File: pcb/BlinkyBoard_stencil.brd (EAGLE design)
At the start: 25.2 x 10 mm, 23 parts, among them Q1 16 MHz

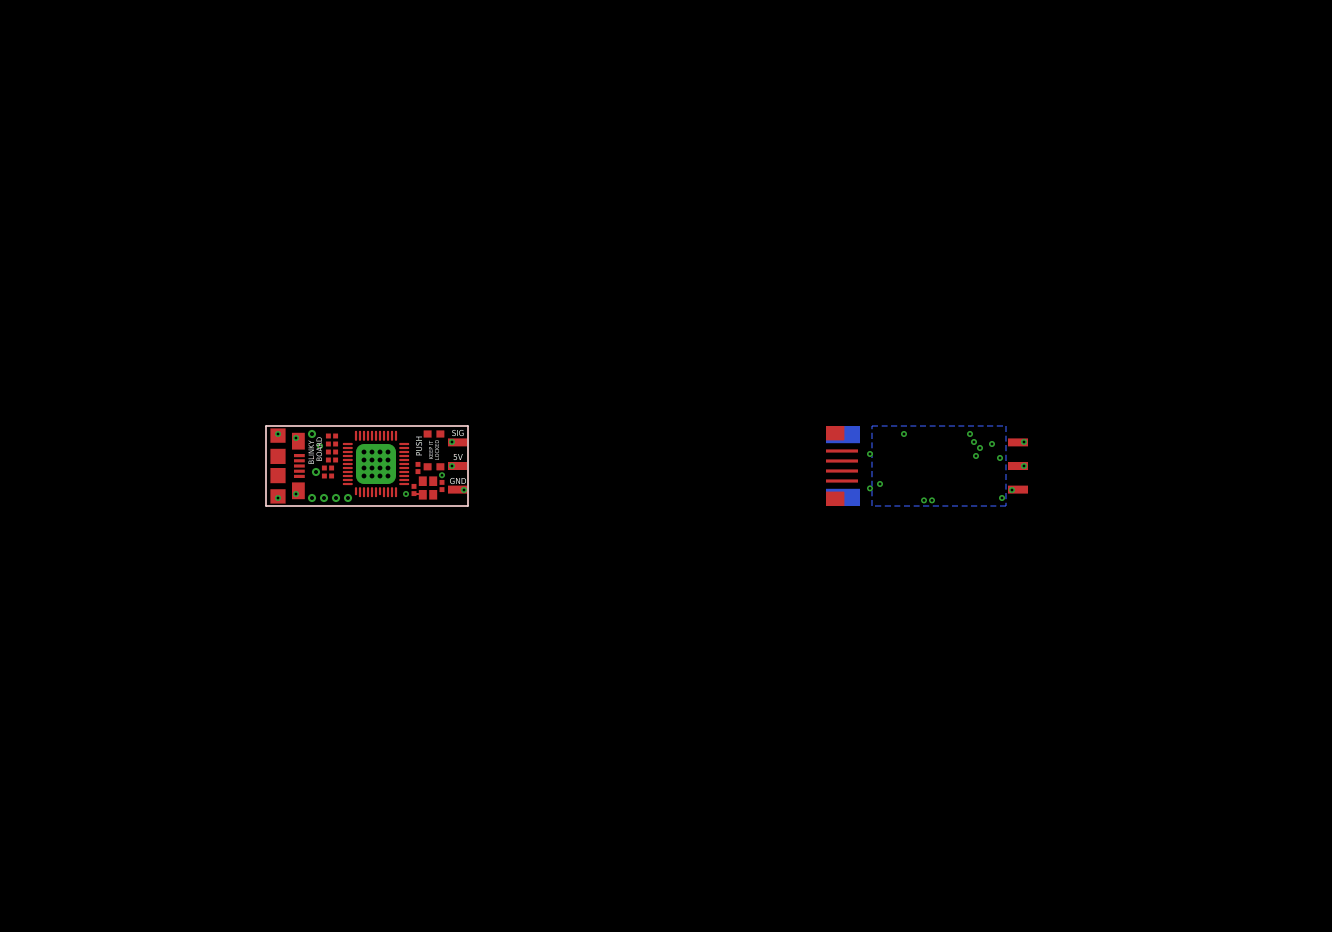
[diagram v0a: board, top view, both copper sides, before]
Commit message: Fix the stencil: use drill holes from Zach's library
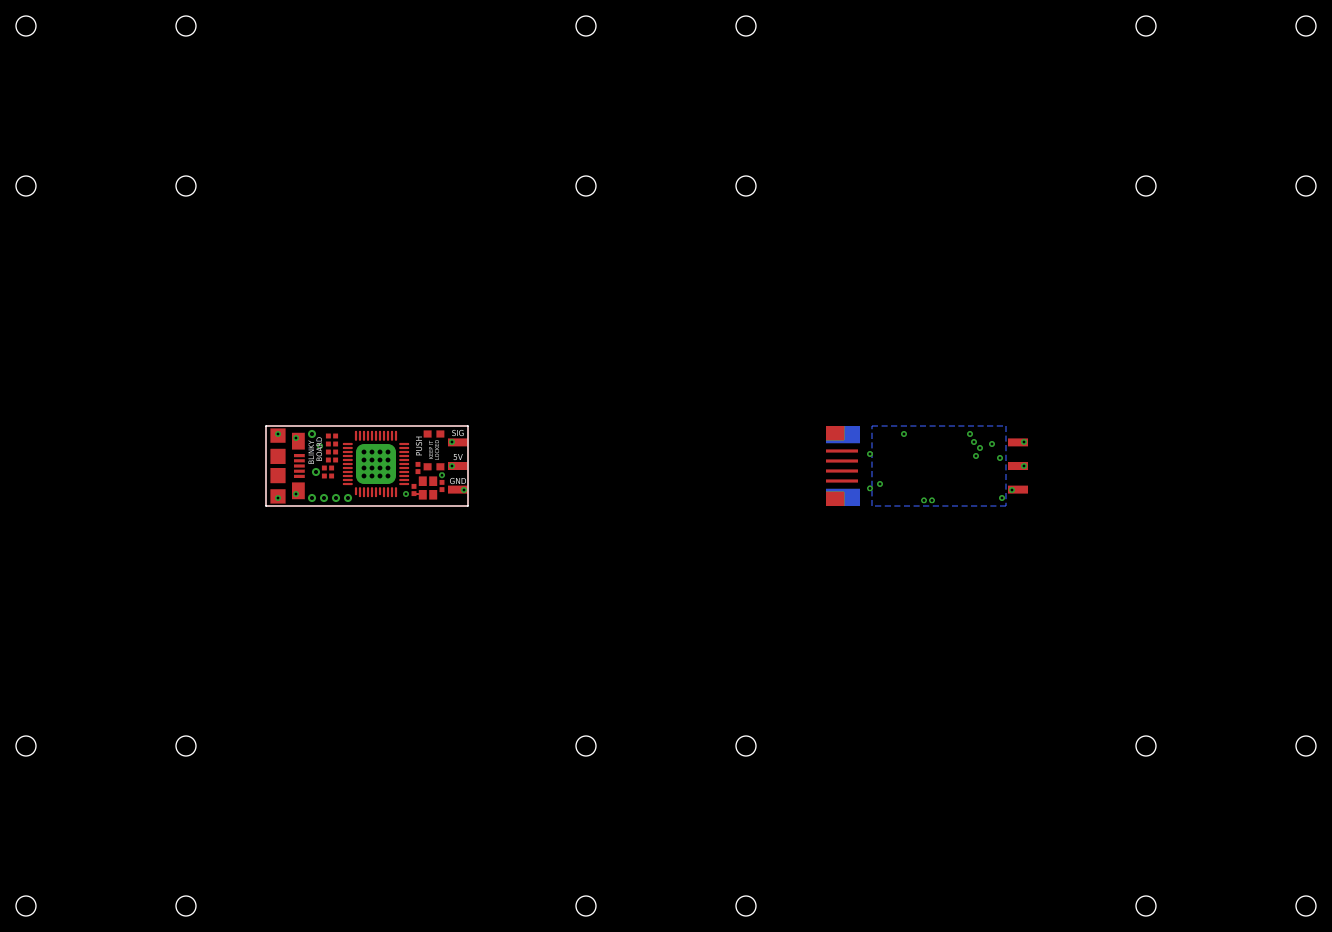
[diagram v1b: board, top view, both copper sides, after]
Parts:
- added E$1, E$10, E$11, E$12, E$13, E$14, E$15, E$16, E$17, E$18, E$19, E$2, E$20, E$21, E$22, E$23, E$24, E$3, E$4, E$5, E$6, E$7, E$8, E$9: (no value), Hoektronics:ALIGNMENT-HOLE-2.5MM
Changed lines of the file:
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@@
 LOCKED</text>
 <text x="13.75" y="2.25" size="0.8128" layer="26" font="vector" ratio="20" rot="MR0" align="center">blinkiverse.com/bb</text>
-<circle x="-30" y="-30" radius="1.25" width="0.05" layer="31"/>
-<circle x="-10" y="-30" radius="1.15" width="0.05" layer="31"/>
-<circle x="-10" y="-50" radius="1.2" width="0.05" layer="31"/>
-<circle x="-30" y="-50" radius="1.2" width="0.05" layer="31"/>
-<circle x="40" y="-30" radius="1.25" width="0.05" layer="31"/>
-<circle x="60" y="-30" radius="1.15" width="0.05" layer="31"/>
-<circle x="60" y="-50" radius="1.2" width="0.05" layer="31"/>
-<circle x="40" y="-50" radius="1.2" width="0.05" layer="31"/>
-<circle x="110" y="-30" radius="1.25" width="0.05" layer="31"/>
-<circle x="130" y="-30" radius="1.15" width="0.05" layer="31"/>
-<circle x="130" y="-50" radius="1.2" width="0.05" layer="31"/>
-<circle x="110" y="-50" radius="1.2" width="0.05" layer="31"/>
-<circle x="-30" y="60" radius="1.25" width="0.05" layer="31"/>
-<circle x="-10" y="60" radius="1.15" width="0.05" layer="31"/>
-<circle x="-10" y="40" radius="1.2" width="0.05" layer="31"/>
-<circle x="-30" y="40" radius="1.2" width="0.05" layer="31"/>
-<circle x="40" y="60" radius="1.25" width="0.05" layer="31"/>
-<circle x="60" y="60" radius="1.15" width="0.05" layer="31"/>
-<circle x="60" y="40" radius="1.2" width="0.05" layer="31"/>
-<circle x="40" y="40" radius="1.2" width="0.05" layer="31"/>
-<circle x="110" y="60" radius="1.25" width="0.05" layer="31"/>
-<circle x="130" y="60" radius="1.15" width="0.05" layer="31"/>
-<circle x="130" y="40" radius="1.2" width="0.05" layer="31"/>
-<circle x="110" y="40" radius="1.2" width="0.05" layer="31"/>
 </plain>
 <attributes>
@@
 <element name="JP1" library="blinkiverse" package="SMT_PAD-5.5MM-4" value="" x="72" y="5" rot="R90"/>
 <element name="U$9" library="blinkiverse" package="OSHW-LOGO-M" value="" x="89" y="5" rot="MR0"/>
+<element name="E$1" library="Hoektronics" package="ALIGNMENT-HOLE-2.5MM" value="" x="-30" y="-50"/>
+<element name="E$2" library="Hoektronics" package="ALIGNMENT-HOLE-2.5MM" value="" x="-10" y="-50"/>
+<element name="E$3" library="Hoektronics" package="ALIGNMENT-HOLE-2.5MM" value="" x="-10" y="-30"/>
+<element name="E$4" library="Hoektronics" package="ALIGNMENT-HOLE-2.5MM" value="" x="-30" y="-30"/>
+<element name="E$5" library="Hoektronics" package="ALIGNMENT-HOLE-2.5MM" value="" x="40" y="-50"/>
+<element name="E$6" library="Hoektronics" package="ALIGNMENT-HOLE-2.5MM" value="" x="60" y="-50"/>
+<element name="E$7" library="Hoektronics" package="ALIGNMENT-HOLE-2.5MM" value="" x="60" y="-30"/>
+<element name="E$8" library="Hoektronics" package="ALIGNMENT-HOLE-2.5MM" value="" x="40" y="-30"/>
+<element name="E$9" library="Hoektronics" package="ALIGNMENT-HOLE-2.5MM" value="" x="110" y="-50"/>
+<element name="E$10" library="Hoektronics" package="ALIGNMENT-HOLE-2.5MM" value="" x="130" y="-50"/>
+<element name="E$11" library="Hoektronics" package="ALIGNMENT-HOLE-2.5MM" value="" x="130" y="-30"/>
+<element name="E$12" library="Hoektronics" package="ALIGNMENT-HOLE-2.5MM" value="" x="110" y="-30"/>
+<element name="E$13" library="Hoektronics" package="ALIGNMENT-HOLE-2.5MM" value="" x="-30" y="40"/>
+<element name="E$14" library="Hoektronics" package="ALIGNMENT-HOLE-2.5MM" value="" x="-10" y="40"/>
+<element name="E$15" library="Hoektronics" package="ALIGNMENT-HOLE-2.5MM" value="" x="-10" y="60"/>
+<element name="E$16" library="Hoektronics" package="ALIGNMENT-HOLE-2.5MM" value="" x="-30" y="60"/>
+<element name="E$17" library="Hoektronics" package="ALIGNMENT-HOLE-2.5MM" value="" x="40" y="40"/>
+<element name="E$18" library="Hoektronics" package="ALIGNMENT-HOLE-2.5MM" value="" x="60" y="40"/>
+<element name="E$19" library="Hoektronics" package="ALIGNMENT-HOLE-2.5MM" value="" x="60" y="60"/>
+<element name="E$20" library="Hoektronics" package="ALIGNMENT-HOLE-2.5MM" value="" x="40" y="60"/>
+<element name="E$21" library="Hoektronics" package="ALIGNMENT-HOLE-2.5MM" value="" x="110" y="40"/>
+<element name="E$22" library="Hoektronics" package="ALIGNMENT-HOLE-2.5MM" value="" x="130" y="40"/>
+<element name="E$23" library="Hoektronics" package="ALIGNMENT-HOLE-2.5MM" value="" x="130" y="60"/>
+<element name="E$24" library="Hoektronics" package="ALIGNMENT-HOLE-2.5MM" value="" x="110" y="60"/>
 </elements>
 <signals>
